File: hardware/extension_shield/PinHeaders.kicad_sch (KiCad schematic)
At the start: 6 parts, among them J1 SSQ-108-03-T-D, J2 SSQ-110-03-T-D, J3 SSQ-108-03-T-D, J4 SSQ-106-03-T-D, J8 SSQ-114-03-T-D, J9 SSQ-116-03-T-D

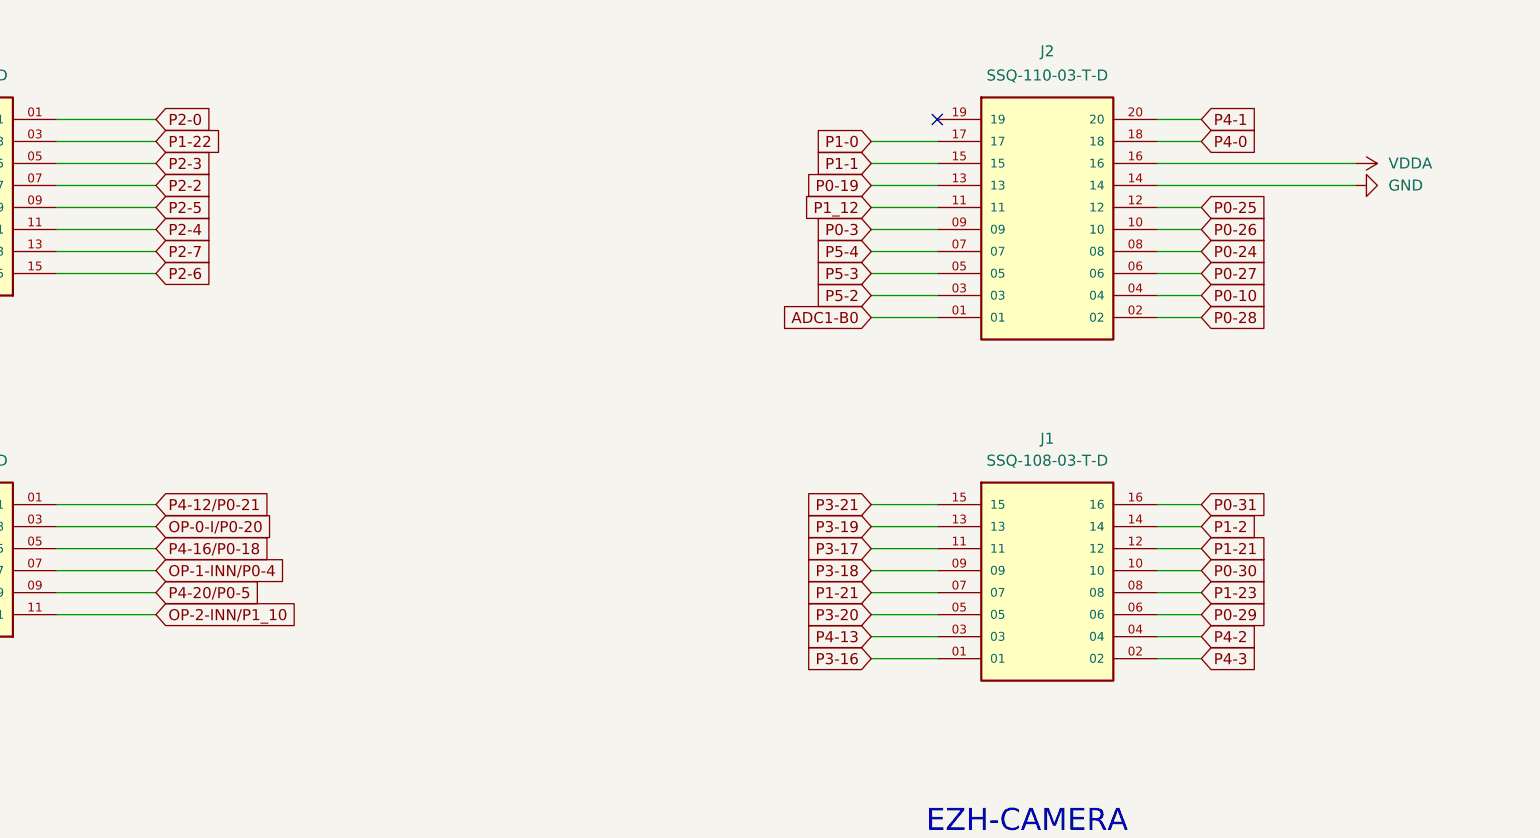
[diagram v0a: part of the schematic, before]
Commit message: [HW] Adds Labels To Expansion Shield Schematic, PDF Schematic & Performed Schematic, PCB Tests.
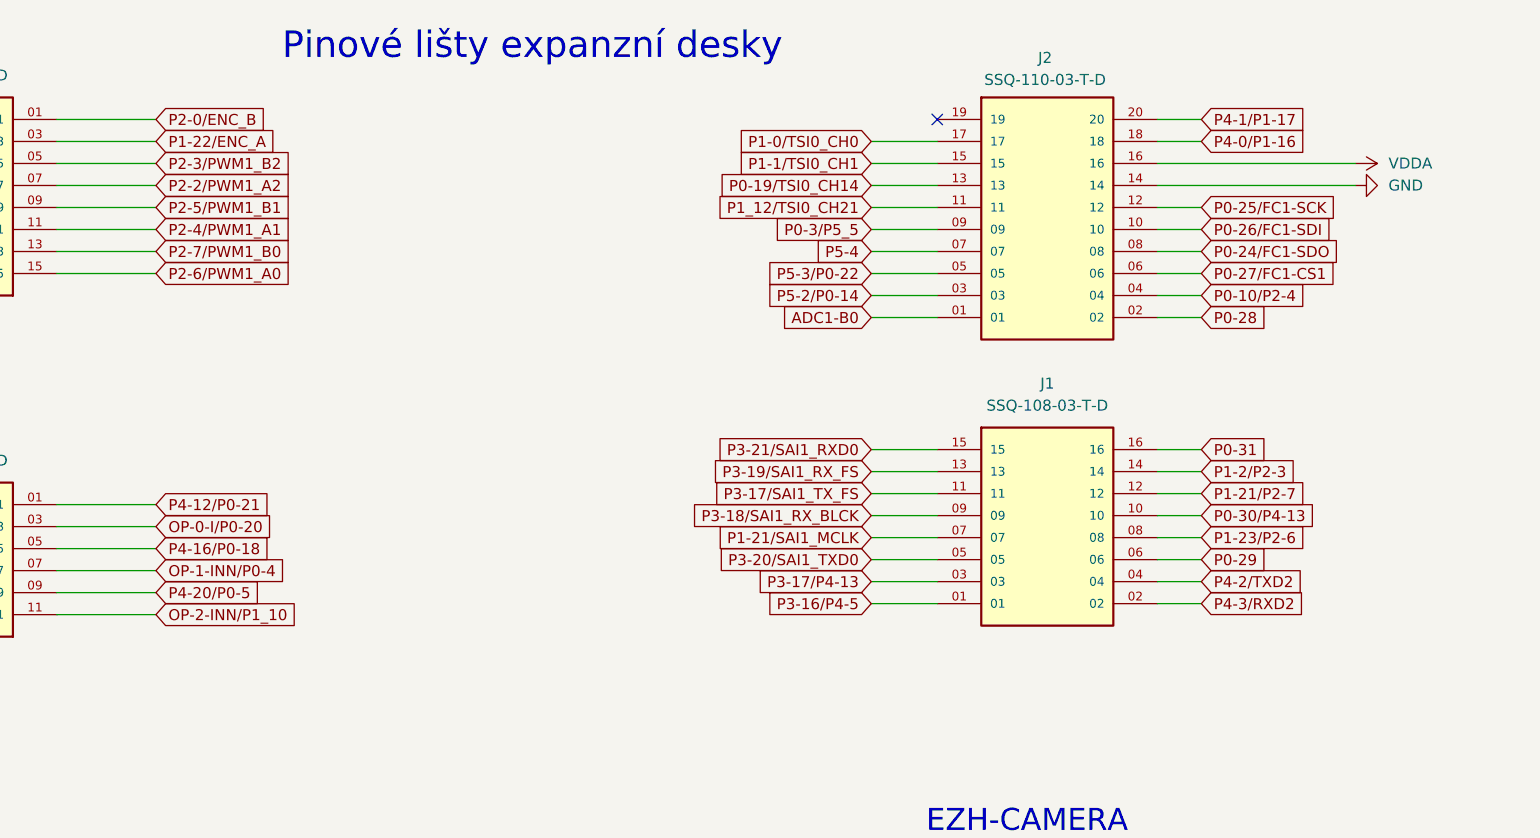
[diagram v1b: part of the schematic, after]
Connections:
- net P0-10 renamed P0-10/P2-4
- net P0-19 renamed P0-19/TSI0_CH14
- net P0-24 renamed P0-24/FC1-SDO
- net P0-25 renamed P0-25/FC1-SCK
- net P0-26 renamed P0-26/FC1-SDI
- net P0-27 renamed P0-27/FC1-CS1
- net P0-3 renamed P0-3/P5_5
- net P0-30 renamed P0-30/P4-13
- net P1-0 renamed P1-0/TSI0_CH0
- net P1-1 renamed P1-1/TSI0_CH1
- net P1-2 renamed P1-2/P2-3
- net P1-21 renamed P1-21/P2-7
- net P1-21/P2-7: no longer J1.07
- net P1-22 renamed P1-22/ENC_A
- net P1-23 renamed P1-23/P2-6
- net P1_12 renamed P1_12/TSI0_CH21
- net P2-0 renamed P2-0/ENC_B
- net P2-2 renamed P2-2/PWM1_A2
- net P2-3 renamed P2-3/PWM1_B2
- net P2-4 renamed P2-4/PWM1_A1
- net P2-5 renamed P2-5/PWM1_B1
- net P2-6 renamed P2-6/PWM1_A0
- net P2-7 renamed P2-7/PWM1_B0
- net P3-16 renamed P3-16/P4-5
- net P3-17 renamed P3-17/SAI1_TX_FS
- net P3-18 renamed P3-18/SAI1_RX_BLCK
- net P3-19 renamed P3-19/SAI1_RX_FS
- net P3-20 renamed P3-20/SAI1_TXD0
- net P3-21 renamed P3-21/SAI1_RXD0
- net P4-0 renamed P4-0/P1-16
- net P4-1 renamed P4-1/P1-17
- net P4-13 renamed P3-17/P4-13
- net P4-2 renamed P4-2/TXD2
- net P4-3 renamed P4-3/RXD2
- net P5-2 renamed P5-2/P0-14
- net P5-3 renamed P5-3/P0-22
- new net P1-21/SAI1_MCLK: J1.07
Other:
- note added: "Pinové lišty expanzní desky"
- title: Datalogger Expansion Shield -> Data Logger Expansion Shield
- moved on the sheet: J1
